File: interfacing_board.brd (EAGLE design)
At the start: 74.9 x 77.1 mm, 73 parts, among them IC1 AD817, IC2 AD817, IC3 AD817, IC4 AD817, IC5 AD817, IC8 AD817, X1 87758-3816, X2 87758-3816, X4 22-23-2081

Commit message: Rev1.9. Small board, autorouted. Too thin routes. For SED2.0
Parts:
- removed ALBIN1, ALBIN2: 22-05-7028-02, EP_molex_6410_7395:7395-02
- removed C7, C8: 0.1uF, capacitor-wima:C2.5-2
- removed IC1, IC2, IC3, IC4, IC5, IC8: AD817, analog-devices:SO8
- removed OPTO2, OPTO3, OPTO4: 332-04, con-garry:332-04
- removed R24, R30, R33: 1k, eagle-ltspice:0207/10
- removed R26, R31, R34: 10k, eagle-ltspice:0207/10
- removed R29, R32, R7: 100, eagle-ltspice:0207/10
- added ALB1, ALB2: 22-05-7028-02, EP_molex_6410_7395:7395-02
- added C3, C4: 0.1uF, capacitor-wima:C2.5-2
- added IC10, IC11, IC12, IC6, IC7, IC9: AD817, analog-devices:SO8
- added LEVEL_TRANSLATOR: 74LVC8T245, 74lvc8t245:TSSOP24
- added OPTO5, OPTO6, OPTO7: 332-04, con-garry:332-04
- added R1, R2, R3, R39, R4, R40, R41, R42, R43, R44, R45, R46, R47, R48, R49, R50, R51, R52, R53, R54, R55, R56, R57, R58: (no value), adafruit:M0805
- added R59: 2k, eagle-ltspice:0207/10
- added R60, R61, R62, R63, R64, R65, R66, R67: (no value), resistor:M0805
- added U$3, U$4, U$5, U$6, U$7: LMC6001, customy:DIL08
- R23: value 2k -> (none); device eagle-ltspice:0207/10 -> resistor:M0805
- R25: value 10k -> (none); device eagle-ltspice:0207/10 -> resistor:M0805
- R5: value 100 -> (none); device eagle-ltspice:0207/10 -> resistor:M0805
- R6: value 1k -> (none); device eagle-ltspice:0207/10 -> resistor:M0805
- U$2: value 74LVC8T245 -> LMC6001; device 74lvc8t245:TSSOP24 -> customy:DIL08
- moved U$2 1276.3 mm to (59.7, 38.1), turned to 270 degrees
- moved R28 1015.6 mm to (21.6, 45.7), turned to 180 degrees
- moved R19 1009.1 mm to (16.5, 67.3), turned to 90 degrees
- moved R18 1007.9 mm to (44.5, 78.7), turned to 90 degrees
- moved R27 1002.4 mm to (36.8, 45.7), turned to 180 degrees
- moved R25 852.7 mm to (16.5, 87.6), turned to 90 degrees
- moved R6 810.6 mm to (10.2, 87.6), turned to 270 degrees
- moved R5 796.5 mm to (7.62, 87.6), turned to 270 degrees
- moved R23 607.1 mm to (12.7, 87.6), turned to 90 degrees
- moved R22 588.3 mm to (44.5, 66.0), turned to 90 degrees
- moved R21 541.1 mm to (40.6, 78.7), turned to 90 degrees
- moved C6 464.1 mm to (57.1, 27.9), turned to 270 degrees
- moved C5 433.3 mm to (52.1, 27.9), turned to 270 degrees
- moved R20 404.3 mm to (66.0, 29.2), turned to 270 degrees
- moved R14 281.6 mm to (30.5, 67.3), turned to 90 degrees
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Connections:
- net N$24 renamed OL-GRN
- net N$25 renamed OL-BLK
- net N$26 renamed ADC-ADDR
- net N$31 renamed ADC-ALRT
- net N$33 renamed DRV1-VM
- net N$56 renamed DRV2-VM
- net PC1 renamed ADC12_IN9
- removed net EMPTY: ETHER.3
- removed net EXTADC0: ADC.A0
- removed net EXTADC1: ADC.A1
- removed net EXTADC2: ADC.A2
- removed net EXTADC3: ADC.A3
- removed net M1PWM: X2.37
- removed net M2PWM: X2.38
- removed net N$13: OPTO2.1, R7.1
- removed net N$14: OPTO2.2, R24.1
- removed net N$17: OPTO3.1, R29.1
- removed net N$18: OPTO3.2, R30.1
- removed net N$21: OPTO4.1, R32.1
- removed net N$22: OPTO4.2, R33.1
- removed net N$27: ADC.SDA
- removed net N$28: ADC.SCL
- removed net N$38: ENDR1.5
- removed net N$40: ENDR1.9
- removed net N$42: ENDR1.4
- removed net N$43: ENDR1.6
- removed net N$44: ENDR1.8
- removed net N$45: ENDR1.10
- removed net N$46: ENDR2.1
- removed net N$47: ENDR2.3
- removed net N$48: ENDR2.5
- removed net N$49: ENDR2.7
- removed net N$50: ENDR2.9
- removed net N$51: ENDR2.2
- removed net N$52: ENDR2.4
- removed net N$53: ENDR2.6
- removed net N$54: ENDR2.8
- removed net N$55: ENDR2.10
- removed net PA0: X1.11
- removed net PA1: X1.9
- removed net PA10: X2.6
- removed net PA9: X2.18
- removed net PB10: X2.14
- removed net PB11: X2.21
- removed net PB6: X2.22
- removed net PB7: X1.18
- new net ADC-SCL: ADC.SCL, X1.18
- new net ADC-SDA: ADC.SDA, X2.22
- new net ADC12_IN8: X1.5
- new net CHA-1: IC7.6, LEVEL_TRANSLATOR.21, R41.1
- new net CHA-1L: LEVEL_TRANSLATOR.3
- new net CHA-2: IC11.6, LEVEL_TRANSLATOR.18, R53.1
- new net CHA-2L: LEVEL_TRANSLATOR.6, X1.9
- new net CHB-1: IC6.6, LEVEL_TRANSLATOR.20, R3.1
- new net CHB-1L: LEVEL_TRANSLATOR.4
- new net CHB-2: IC10.6, LEVEL_TRANSLATOR.17, R49.1
- new net CHB-2L: LEVEL_TRANSLATOR.7, X2.14
- new net CHC-1: IC9.6, LEVEL_TRANSLATOR.19, R45.1
- new net CHC-1L: LEVEL_TRANSLATOR.5, X1.11
- new net CHC-2: IC12.6, LEVEL_TRANSLATOR.16, R57.1
- new net CHC-2L: LEVEL_TRANSLATOR.8, X2.21
- new net INCHA-1: ENDR1.6, R40.1
- new net INCHA-2: ENDR2.6, R52.1
- new net INCHB-1: ENDR1.8, R1.1
- new net INCHB-2: ENDR2.8, R47.1
- new net INCHC-1: ENDR1.10, R43.1
- new net INCHC-2: ENDR2.10, R55.1
- new net IND3: OPTO5.1, R61.2
- new net IND4: OPTO7.1, R67.2
- new net N$1: IC6.2, R1.2, R3.2
- new net N$10: IC10.3, R48.2, R50.1
- new net N$15: OPTO6.4, R62.1
- new net N$19: IC11.2, R51.2, R53.2
- new net N$20: IC7.2, R39.2, R41.2
- new net N$29: C3.1, R59.2, U$2.2, UV1.2
- new net N$30: IC7.3, R40.2, R42.1
- new net N$32: IC9.2, R43.2, R45.2
- new net N$34: IC9.3, R44.2, R46.1
- new net N$35: IC11.3, R52.2, R54.1
- new net N$4: IC6.3, R2.2, R4.1
- new net N$9: IC10.2, R47.2, R49.2
- new net OL_RX: OPENLOG.OLRXI, X2.18
- new net OL_TX: OPENLOG.OLTXO, X2.6
- new net ~INCHA-1: ENDR1.5, R39.1
- new net ~INCHA-2: ENDR2.5, R51.1
- new net ~INCHB-1: ENDR1.7, R2.1
- new net ~INCHB-2: ENDR2.7, R48.1
- new net ~INCHC-1: ENDR1.9, R44.1
- new net ~INCHC-2: ENDR2.9, R56.1
- net 3.3V: now also LEVEL_TRANSLATOR.1, R25.2, R60.2, R62.2, R63.2, R65.2, R66.2, U$2.7, U$3.7, U$4.7, U$5.7, U$6.7, U$7.7; no longer IC1.7, IC2.7, IC3.7, IC4.7, IC5.7, IC8.7, R24.2, R29.2, R30.2, R32.2, R33.2, R7.2
- net 5V: now also ENDR1.2, ENDR2.2, IC10.7, IC11.7, IC12.7, IC6.7, IC7.7, IC9.7, LEVEL_TRANSLATOR.23, LEVEL_TRANSLATOR.24
- net ALBEDO1: now also C5.2, C6.2, R21.1, R22.1, U$6.6, U$7.6, X2.5; no longer C1.2, IC5.6, R16.1
- net ALBEDO2: now also X2.33; no longer C2.2, IC8.6, R17.1
- net CS_HTP2: now also X2.37
- net CS_RTC: now also X2.38
- net GND: now also ALB1.1, ALB2.1, ENDR1.3, ENDR2.3, IC10.4, IC11.4, IC12.4, IC6.4, IC7.4, IC9.4, LEVEL_TRANSLATOR.11, LEVEL_TRANSLATOR.12, LEVEL_TRANSLATOR.13, LEVEL_TRANSLATOR.2, LEVEL_TRANSLATOR.22, OPTO1.2, OPTO5.2, OPTO6.2, OPTO7.2, R23.1, R4.2, R42.2, R46.2, R50.2, R54.2, R58.2, R61.1, R64.1, R67.1, U$2.3, U$2.4, U$3.3, U$3.4, U$4.3, U$4.4, U$5.3, U$5.4, U$6.3, U$6.4, U$7.3, U$7.4, UV1.1, UV2.1, VIS1.1, VIS2.1; no longer ALBIN1.2, ALBIN2.2, IC1.3, IC1.4, IC1.8, IC2.3, IC2.4, IC2.8, IC3.3, IC3.4, IC3.8, IC4.3, IC4.4, IC4.8, IC5.3, IC5.4, IC5.8, IC8.3, IC8.4, IC8.8, OPTO1.3, OPTO2.3, OPTO3.3, OPTO4.3, R25.2, R26.2, R31.2, R34.2, UV1.2, UV2.2, VIS1.2, VIS2.2
- net IND1: now also OPTO1.1, R23.2; no longer OPTO1.4, OPTO3.4, R25.1, R31.1
- net IND2: now also OPTO6.1, R64.2; no longer OPTO2.4, OPTO4.4, R26.1, R34.1
- net N$11: now also OPTO5.4, R25.1; no longer OPTO1.1, R5.1
- net N$12: now also OPTO6.3, R63.1; no longer OPTO1.2, R6.1
- net N$16: now also OPTO7.3, R66.1; no longer OPENLOG.OLTXO
- net N$2: now also OPTO1.3, R6.1; no longer ALBIN1.1, C1.1, IC5.2, R16.2
- net N$23: now also OPTO7.4, R65.1; no longer OPENLOG.OLRXI
- net N$3: now also C1.1, R16.2, U$3.2, UV2.2; no longer ALBIN2.1, C2.1, IC8.2, R17.2
- net N$36: now also IC12.2, R55.2, R57.2; no longer ENDR1.1
- net N$37: now also IC12.3, R56.2, R58.1; no longer ENDR1.3
- net N$39: now also ALB1.2, C5.1, R21.2, U$6.2; no longer ENDR1.7
- net N$41: now also ALB2.2, C6.1, R22.2, U$7.2; no longer ENDR1.2
- net N$5: now also OPTO5.3, R60.1; no longer C6.1, IC1.2, R21.2, VIS1.1
- net N$6: now also C2.1, R17.2, U$4.2, VIS1.2; no longer C7.1, IC3.2, R22.2, UV2.1
- net N$7: now also OPTO1.4, R5.1; no longer C8.1, IC4.2, R23.2, VIS2.1
- net N$8: now also C4.1, U$5.2, VIS2.2; no longer C5.1, IC2.2, UV1.1
- net UV1: now also ADC.A0, C3.2, R59.1, U$2.6; no longer C5.2, IC2.6, R20.1, X2.5
- net UV2: now also ADC.A1, C1.2, R16.1, U$3.6; no longer C7.2, IC3.6, R22.1, X2.33
- net VIS1: now also ADC.A2, C2.2, R17.1, U$4.6; no longer C6.2, IC1.6, R21.1, X1.5
- net VIS2: now also ADC.A3, C4.2, R20.1, U$5.6; no longer C8.2, IC4.6, R23.1
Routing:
- net GND: track 0.00 -> 601.8 mm, vias 0 -> 3
- net 3.3V: track 0.00 -> 406.9 mm, vias 0 -> 4
- net SPI2_SCK: track 0.00 -> 223.6 mm, vias 0 -> 5
- net 5V: track 0.00 -> 190.8 mm, vias 0 -> 5
- net N$32: track 0.00 -> 184.8 mm, vias 0 -> 4
- net SPI2_MISO: track 0.00 -> 183.5 mm, vias 0 -> 6
- net SPI2_MOSI: track 0.00 -> 177.1 mm, vias 0 -> 3
- net CS_HTP2: track 0.00 -> 167.9 mm, vias 0 -> 4
- net N$3: track 0.00 -> 166.9 mm, vias 0 -> 1
- net INCHB-2: track 0.00 -> 148.2 mm, vias 0 -> 1
- net N$39: track 0.00 -> 132.5 mm, vias 0 -> 2
- net M12: track 0.00 -> 131.4 mm, vias 0 -> 3
- net CS_RTC: track 0.00 -> 129.2 mm, vias 0 -> 2
- net ~INCHB-1: track 0.00 -> 126.3 mm, vias 0 -> 4
- net VIS2: track 0.00 -> 125.9 mm, vias 0 -> 3
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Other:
- board size 74.9 x 77.1 mm -> 85.1 x 77.1 mm

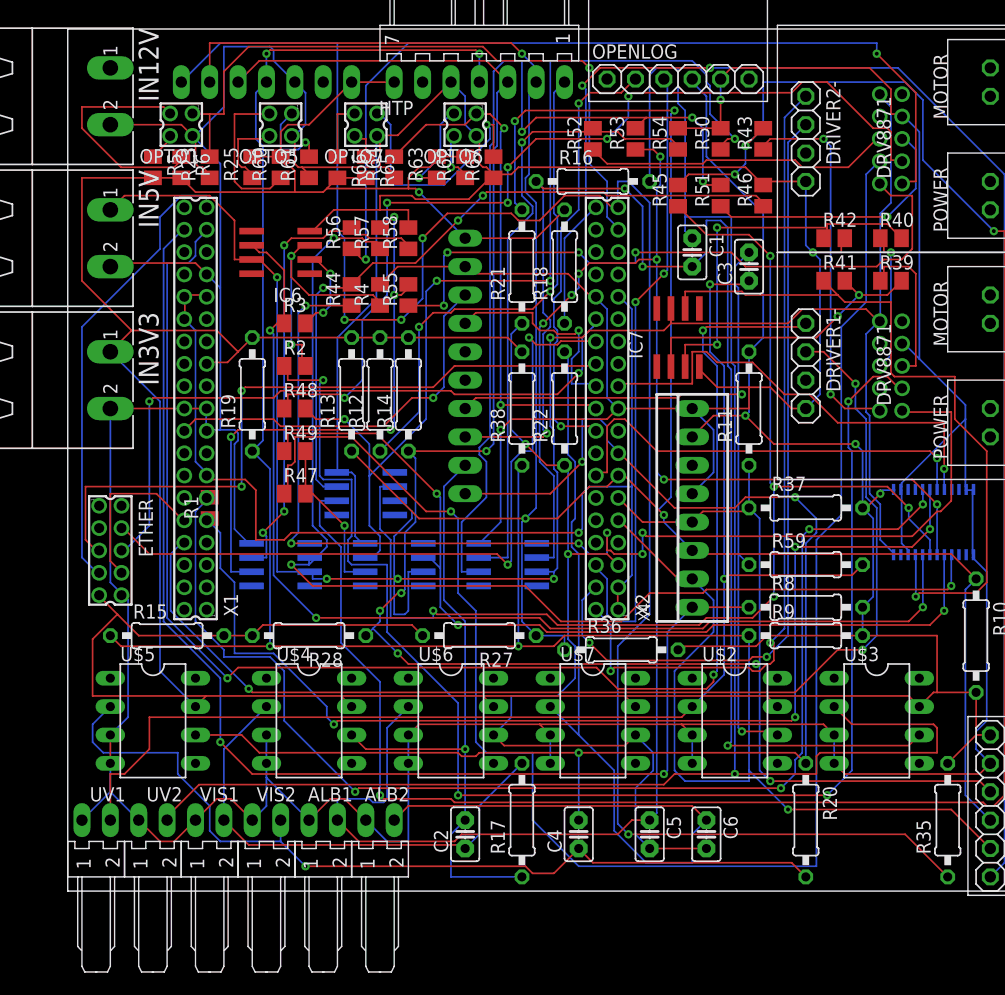
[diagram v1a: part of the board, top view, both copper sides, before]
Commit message: deleted photodiode sockets and their amplifiers on interfacing board schematic and PCB
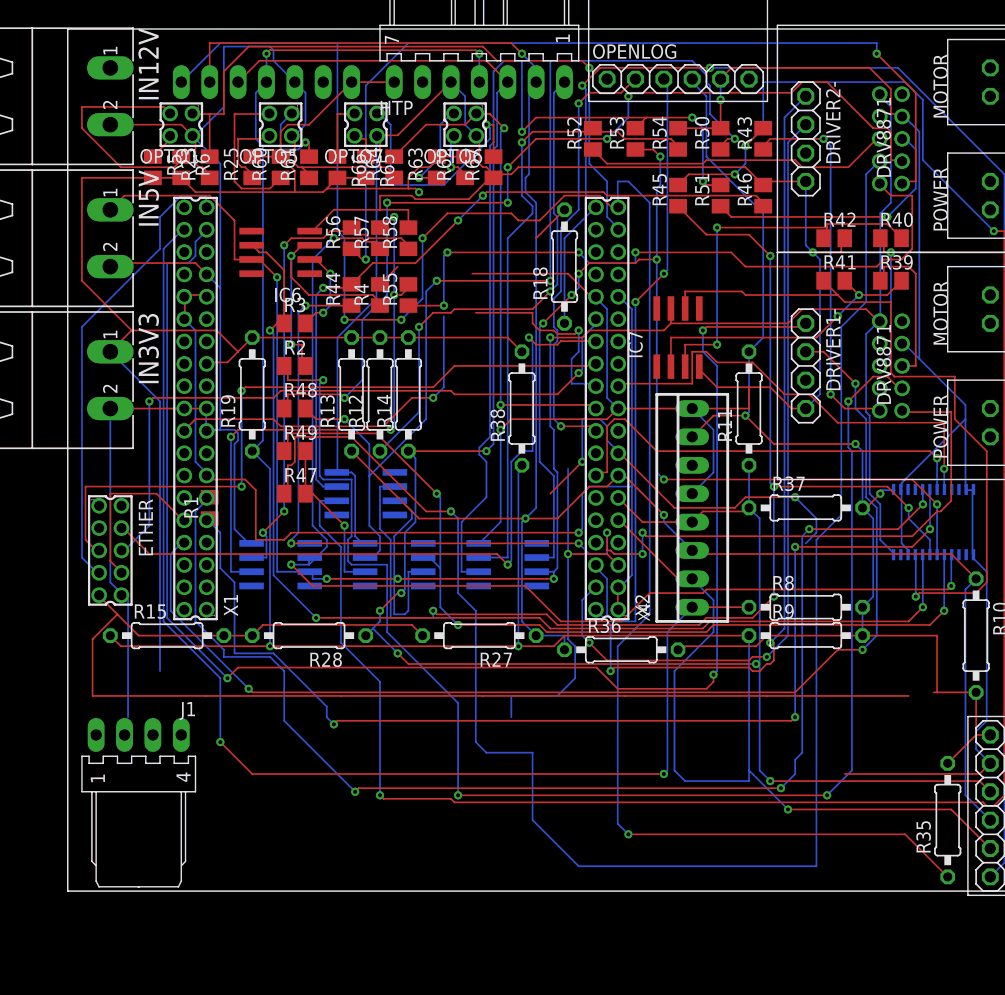
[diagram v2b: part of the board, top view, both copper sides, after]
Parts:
- removed ADC: ADS1015, SKA_EP_molex_6410_7395:EXADC
- removed ALB1, ALB2, UV1, UV2, VIS1, VIS2: 22-05-7028-02, EP_molex_6410_7395:7395-02
- removed C1, C2, C3, C4, C5, C6: 0.1uF, capacitor-wima:C2.5-2
- removed R16, R17, R20, R21, R22, R59: 2k, eagle-ltspice:0207/10
- removed U$2, U$3, U$4, U$5, U$6, U$7: LMC6001, customy:DIL08
- added J1: 22-05-7048-04, EP_molex_6410_7395:7395-04
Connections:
- net ALBEDO2 renamed PC5
- removed net ADC-ADDR: ADC.ADDR
- removed net ADC-ALRT: ADC.ALRT
- removed net ADC-SCL: ADC.SCL, X1.18
- removed net ADC-SDA: ADC.SDA, X2.22
- removed net ALBEDO1: C5.2, C6.2, R21.1, R22.1, U$6.6, U$7.6, X2.5
- removed net N$29: C3.1, R59.2, U$2.2, UV1.2
- removed net N$3: C1.1, R16.2, U$3.2, UV2.2
- removed net N$39: ALB1.2, C5.1, R21.2, U$6.2
- removed net N$41: ALB2.2, C6.1, R22.2, U$7.2
- removed net N$6: C2.1, R17.2, U$4.2, VIS1.2
- removed net N$8: C4.1, R20.2, U$5.2, VIS2.2
- removed net UV1: ADC.A0, C3.2, R59.1, U$2.6
- removed net UV2: ADC.A1, C1.2, R16.1, U$3.6
- removed net VIS1: ADC.A2, C2.2, R17.1, U$4.6
- removed net VIS2: ADC.A3, C4.2, R20.1, U$5.6, X2.15
- new net PC4: X2.5
- new net SCL1: X2.22
- new net SDA1: X1.18
- new net VIS2<<<<<<<<<<: X2.15
- net 3.3V: no longer ADC.VDD, U$2.7, U$3.7, U$4.7, U$5.7, U$6.7, U$7.7
- net GND: no longer ADC.GND, ALB1.1, ALB2.1, U$2.3, U$2.4, U$3.3, U$3.4, U$4.3, U$4.4, U$5.3, U$5.4, U$6.3, U$6.4, U$7.3, U$7.4, UV1.1, UV2.1, VIS1.1, VIS2.1
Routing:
- net N$3: track 166.9 -> 0.00 mm, vias 1 -> 0
- net N$39: track 132.5 -> 0.00 mm, vias 2 -> 0
- net VIS2: track 125.9 -> 0.00 mm, vias 3 -> 0
- net UV2: track 122.2 -> 0.00 mm, vias 4 -> 0
- net GND: track 601.8 -> 482.2 mm
- net N$29: track 116.4 -> 0.00 mm, vias 2 -> 0
- net N$41: track 90.1 -> 0.00 mm
- net ALBEDO1: track 81.4 -> 0.00 mm, vias 2 -> 0
- net N$8: track 78.8 -> 0.00 mm, vias 1 -> 0
- net UV1: track 73.9 -> 0.00 mm, vias 2 -> 0
- net VIS1: track 56.0 -> 0.00 mm, vias 1 -> 0
- net N$6: track 44.1 -> 0.00 mm
- net VIS2<<<<<<<<<<: track 0.00 -> 36.7 mm, vias 0 -> 2
- net ADC-SCL: track 34.4 -> 0.00 mm, vias 1 -> 0
- net PC4: track 0.00 -> 32.2 mm, vias 0 -> 1
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
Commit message: updated pullups
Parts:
- removed IC10, IC11, IC12, IC6, IC7, IC9: AD817, analog-devices:SO8
- removed LEVEL_TRANSLATOR: 74LVC8T245, 74lvc8t245:TSSOP24
- removed R28, R35, R36, R37, R38: 2k, eagle-ltspice:0207/10
- removed R39, R40, R41, R42, R43, R44, R45, R46, R47, R48, R49, R50, R51, R52, R53, R54, R55, R56, R57, R58: (no value), adafruit:M0805
- added ALBEDO1, ALBEDO2, UV2, VIS1, VIS2: 22-05-7048-04, EP_molex_6410_7395:7395-04
- added IC1, IC2: MAX3096CSE, maxim:SO16
- added R16, R20, R22, R26, R30, R32: 10k, rcl:M0805
- added R17, R21, R24, R29, R31, R7: 5k, rcl:M0805
- R1, R2, R3, R4: value (none) -> 10k; device adafruit:M0805 -> rcl:M0805
- R10, R11, R8, R9: value 2k -> 4.7k; device eagle-ltspice:0207/10 -> rcl:M0805
- R12, R13, R14, R15, R19, R27: value 2k -> 5k; device eagle-ltspice:0207/10 -> rcl:M0805
- moved R9 394.6 mm to (-26.7, -337.8)
- moved R8 390.9 mm to (-26.7, -331.5)
- moved R19 388.5 mm to (-26.7, -318.8), turned to 0 degrees
- moved R14 377.7 mm to (-26.7, -306.1), turned to 0 degrees
- moved R27 376.2 mm to (-26.7, -325.1), turned to 0 degrees
- moved R13 370.7 mm to (-26.7, -299.7), turned to 0 degrees
- moved R12 364.8 mm to (-26.7, -293.4), turned to 0 degrees
- moved R11 363.8 mm to (-26.7, -287.0), turned to 0 degrees
- moved R15 359.9 mm to (-26.7, -312.4)
- moved R10 343.8 mm to (-26.7, -280.7), turned to 0 degrees
- moved R4 155.4 mm to (-21.6, -71.1), turned to 0 degrees
- moved R3 152.2 mm to (-26.7, -71.1)
- moved R2 129.5 mm to (-26.7, -50.8)
- moved R1 109.0 mm to (-26.7, -44.5), turned to 0 degrees
- renumbered J1 to UV1
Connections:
- removed net N$1: IC6.2, R1.2, R3.2
- removed net N$10: IC10.3, R48.2, R50.1
- removed net N$20: IC7.2, R39.2, R41.2
- removed net N$30: IC7.3, R40.2, R42.1
- removed net N$32: IC9.2, R43.2, R45.2
- removed net N$34: IC9.3, R44.2, R46.1
- removed net N$35: IC11.3, R52.2, R54.1
- removed net N$36: IC12.2, R55.2, R57.2
- removed net N$37: IC12.3, R56.2, R58.1
- removed net N$4: IC6.3, R2.2, R4.1
- removed net N$9: IC10.2, R47.2, R49.2
- new net CHB2-L: R29.1, R30.2
- new net N$13: IC2.12, R4.1
- new net N$18: IC1.4, R1.2
- new net N$8: IC2.4, R3.2
- new net SCL2: VIS1.3, VIS2.3
- new net SDA2: VIS1.2, VIS2.2
- net +5V: now also R1.1, R3.1
- net 3.3V: now also ALBEDO1.1, ALBEDO2.1, UV1.1, UV2.1, VIS1.1, VIS2.1; no longer LEVEL_TRANSLATOR.1, R28.2, R35.2, R36.2, R37.2, R38.2
- net 5V: now also IC1.16, IC2.16; no longer IC10.7, IC11.7, IC12.7, IC6.7, IC7.7, IC9.7, LEVEL_TRANSLATOR.23, LEVEL_TRANSLATOR.24
- net CHA-1: now also IC1.3, R7.2; no longer IC7.6, LEVEL_TRANSLATOR.21, R41.1
- net CHA-1L: now also R16.2, R7.1; no longer LEVEL_TRANSLATOR.3
- net CHA-2: now also IC2.3, R24.2; no longer IC11.6, LEVEL_TRANSLATOR.18, R53.1
- net CHA-2L: now also R24.1, R26.2; no longer LEVEL_TRANSLATOR.6
- net CHB-1: now also IC1.5, R17.2; no longer IC6.6, LEVEL_TRANSLATOR.20, R3.1
- net CHB-1L: now also R17.1, R20.2; no longer LEVEL_TRANSLATOR.4
- net CHB-2: now also IC2.5, R29.2; no longer IC10.6, LEVEL_TRANSLATOR.17, R49.1
- net CHB-2L: no longer LEVEL_TRANSLATOR.7
- net CHC-1: now also IC1.11, R21.2; no longer IC9.6, LEVEL_TRANSLATOR.19, R45.1
- net CHC-1L: now also R21.1, R22.2; no longer LEVEL_TRANSLATOR.5
- net CHC-2: now also IC2.11, R31.2; no longer IC12.6, LEVEL_TRANSLATOR.16, R57.1
- net CHC-2L: now also R31.1, R32.2; no longer LEVEL_TRANSLATOR.8
- net CS_HTP: no longer R12.1
- net CS_HTP2: no longer R35.1
- net CS_IMU: no longer R8.1
- net GND: now also ALBEDO1.4, ALBEDO2.4, IC1.8, IC2.8, R16.1, R2.2, R20.1, R22.1, R26.1, R30.1, R32.1, UV1.4, UV2.4, VIS1.4, VIS2.4; no longer IC10.4, IC11.4, IC12.4, IC6.4, IC7.4, IC9.4, LEVEL_TRANSLATOR.11, LEVEL_TRANSLATOR.12, LEVEL_TRANSLATOR.13, LEVEL_TRANSLATOR.2, LEVEL_TRANSLATOR.22, R42.2, R46.2, R50.2, R54.2, R58.2
- net INCHA-1: now also IC1.2; no longer R40.1
- net INCHA-2: now also IC2.2; no longer R52.1
- net INCHB-1: now also IC1.6; no longer R1.1
- net INCHB-2: now also IC2.6; no longer R47.1
- net INCHC-1: now also IC1.10; no longer R43.1
- net INCHC-2: now also IC2.10; no longer R55.1
- net N$19: now also IC1.12, R2.1; no longer IC11.2, R51.2, R53.2
- net SCL1: now also ALBEDO1.3, ALBEDO2.3, R11.1, UV1.3, UV2.3
- net SDA1: now also ALBEDO1.2, ALBEDO2.2, R10.1, UV1.2, UV2.2
- net SPI1_MISO: now also R13.1
- net SPI1_MOSI: now also R12.1
- net SPI1_SCK: now also R14.1
- net SPI2_MISO: now also R19.1; no longer R11.1, R14.1, R28.1, R37.1
- net SPI2_MOSI: now also R15.1; no longer R10.1, R13.1, R27.1, R36.1
- net SPI2_SCK: now also R27.1; no longer R15.1, R19.1, R38.1, R9.1
- net ~INCHA-1: now also IC1.1; no longer R39.1
- net ~INCHA-2: now also IC2.1; no longer R51.1
- net ~INCHB-1: now also IC1.7; no longer R2.1
- net ~INCHB-2: now also IC2.7; no longer R48.1
- net ~INCHC-1: now also IC1.9; no longer R44.1
- net ~INCHC-2: now also IC2.9; no longer R56.1
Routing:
- net GND: track 482.2 -> 0.00 mm, vias 3 -> 0
- net 3.3V: track 380.3 -> 0.00 mm, vias 4 -> 0
- net SPI2_SCK: track 223.6 -> 0.00 mm, vias 5 -> 0
- net 5V: track 190.8 -> 0.00 mm, vias 5 -> 0
- net N$32: track 184.8 -> 0.00 mm, vias 4 -> 0
- net SPI2_MISO: track 183.5 -> 0.00 mm, vias 6 -> 0
- net SPI2_MOSI: track 177.1 -> 0.00 mm, vias 3 -> 0
- net CS_HTP2: track 167.9 -> 0.00 mm, vias 4 -> 0
- net INCHB-2: track 148.2 -> 0.00 mm, vias 1 -> 0
- net M12: track 131.4 -> 0.00 mm, vias 3 -> 0
- net CS_RTC: track 129.2 -> 0.00 mm, vias 2 -> 0
- net ~INCHB-1: track 126.3 -> 0.00 mm, vias 4 -> 0
- net CS_IMU: track 110.7 -> 0.00 mm, vias 2 -> 0
- net CHC-1L: track 109.9 -> 0.00 mm, vias 4 -> 0
- net CHC-1: track 108.5 -> 0.00 mm, vias 5 -> 0
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
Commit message: BIPOP updated. Grid errors corrected, pull-ups for CS pins added.
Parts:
- removed HTP: 22-05-7078-07, EP_molex_6410_7395:7395-07
- removed R8: 4.7k, rcl:M0805
- removed U$1: RTC_WAVESHARE, SKA_EP_molex_6410_7395:RTC
- removed X4: 22-23-2081, con-molex:22-23-2081
- added HTP2: 22-27-2071-07, EP_molex_6410_7395:6410-07
- added IMU: 22-27-2081-08, EP_molex_6410_7395:6410-08
- added R28, R33: 4.7k, rcl:M0805
- added RTC_: RTC_WAVESHARE, SKA_EP_molex_6410_7395:RTC
- HTP1: value 22-05-7078-07 -> 22-27-2071-07; device EP_molex_6410_7395:7395-07 -> EP_molex_6410_7395:6410-07
- moved R9 388.7 mm to (81.3, 35.6)
- moved R14 384.9 mm to (27.9, 74.9)
- moved R12 381.9 mm to (24.1, 85.1), turned to 180 degrees
- moved R27 380.1 mm to (81.3, 39.4)
- moved R11 374.5 mm to (15.2, 85.1), turned to 90 degrees
- moved R19 371.1 mm to (74.9, 38.1)
- moved R15 360.1 mm to (74.9, 33.0)
- moved R13 345.5 mm to (3.81, 44.5)
- moved R10 324.0 mm to (3.81, 41.9), turned to 180 degrees
- moved VIS2 277.7 mm to (40.6, 36.8), turned to 180 degrees
- moved VIS1 253.1 mm to (29.2, 36.8), turned to 180 degrees
- moved ALBEDO2 232.6 mm to (63.5, 36.8), turned to 180 degrees
- moved ALBEDO1 207.3 mm to (52.1, 36.8), turned to 180 degrees
- moved UV2 168.6 mm to (17.8, 36.8), turned to 180 degrees
- moved IC2 153.3 mm to (35.6, 81.3), turned to 270 degrees
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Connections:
- net VIS2<<<<<<<<<< renamed PB1
- net 3.3V: now also HTP2.7, IMU.7, R28.2, R33.2, RTC_.VCC; no longer HTP.7, R8.2, U$1.VCC, X4.7
- net 3V_O: now also HTP1.6; no longer HTP.6
- net 3V_O2: now also HTP2.6; no longer HTP1.6
- net CS_HTP: now also HTP1.1, R9.1; no longer HTP.1
- net CS_HTP2: now also HTP2.1, R28.1; no longer HTP1.1
- net CS_IMU: now also IMU.1, R33.1; no longer X4.1
- net CS_RTC: now also RTC_.CS; no longer U$1.CS
- net GND: now also HTP2.5, IMU.5, IMU.8, RTC_.GND; no longer HTP.5, U$1.GND, X4.5, X4.8
- net IMU_INT: now also IMU.6; no longer X4.6
- net SPI2_MISO: now also HTP2.3, IMU.4, RTC_.MISO; no longer HTP.3, U$1.MISO, X4.4
- net SPI2_MOSI: now also HTP2.2, IMU.3, RTC_.MOSI; no longer HTP.2, U$1.MOSI, X4.3
- net SPI2_SCK: now also HTP2.4, IMU.2, RTC_.SCK; no longer HTP.4, U$1.SCK, X4.2
